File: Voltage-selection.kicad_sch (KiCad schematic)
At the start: 8 parts, among them Q4 DMP1045U-7, Q5 DMP1045U-7, Q6 DMP1045U-7, SW5 SSSS213202

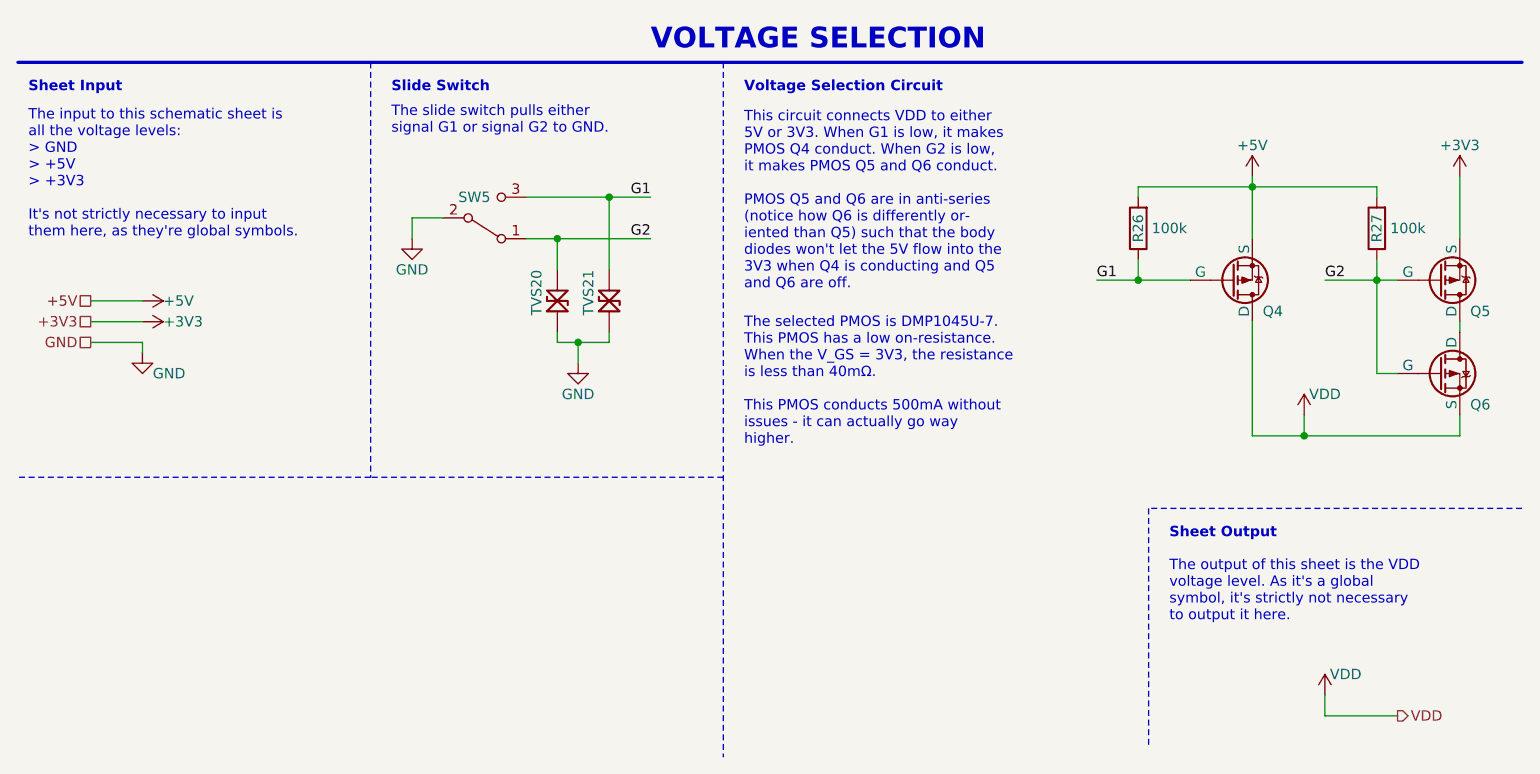
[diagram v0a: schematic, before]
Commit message: Renumber designators and draw new silkscreen
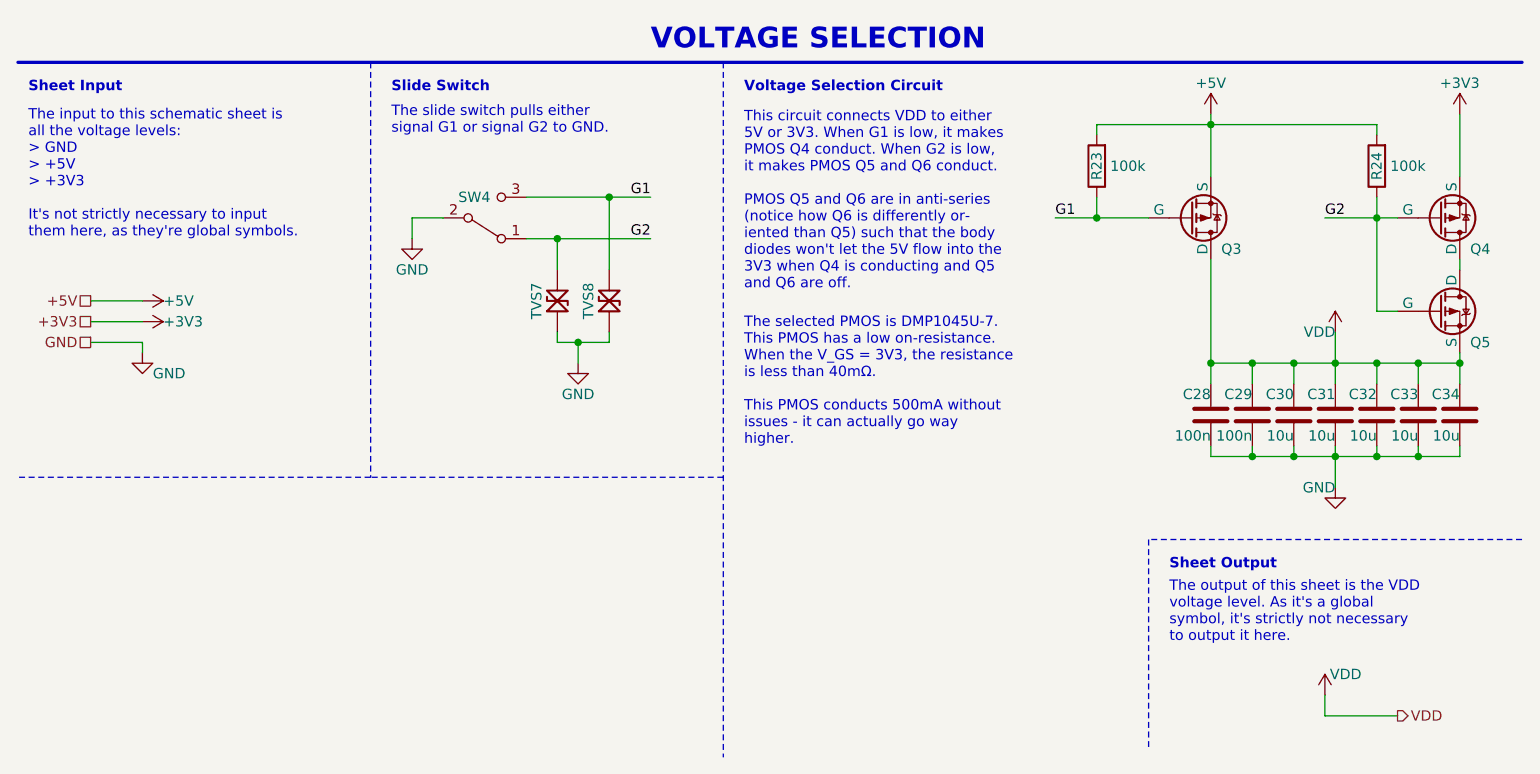
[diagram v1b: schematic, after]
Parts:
- added C28, C29: 100n, Capacitor_SMD:C_0402_1005Metric_Pad0.74x0.62mm_HandSolder, symbol Device:C
- added C30, C31, C32, C33, C34: 10u, Capacitor_SMD:C_0805_2012Metric, symbol Device:C
- renumbered Q4 to Q3, Q5 to Q4, Q6 to Q5, R26 to R23, R27 to R24, SW5 to SW4, TVS20 to TVS7, TVS21 to TVS8
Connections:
- net GND: now also C28.2, C29.2, C30.2, C31.2, C32.2, C33.2, C34.2
- net VDD: now also C28.1, C29.1, C30.1, C31.1, C32.1, C33.1, C34.1
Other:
- moved on the sheet: Q3, Q4, Q5, R23, R24

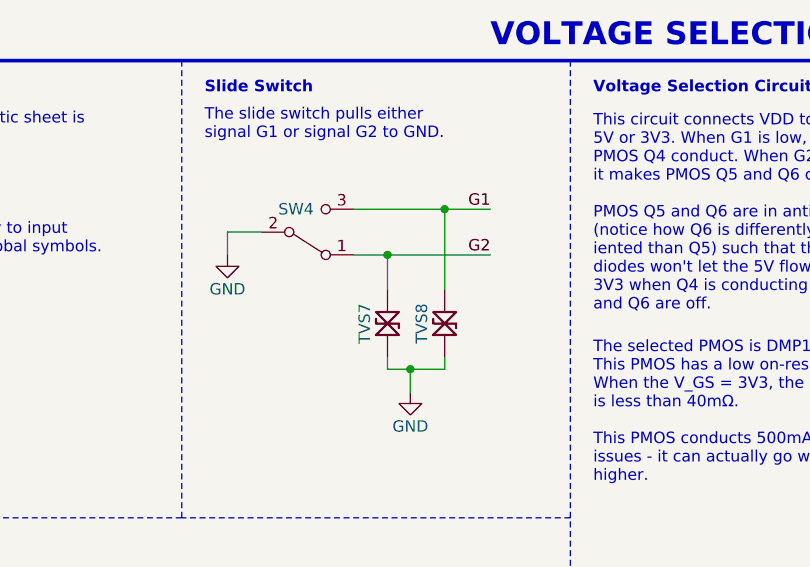
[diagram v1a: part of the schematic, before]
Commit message: Replace TVS diodes with cheaper alternative
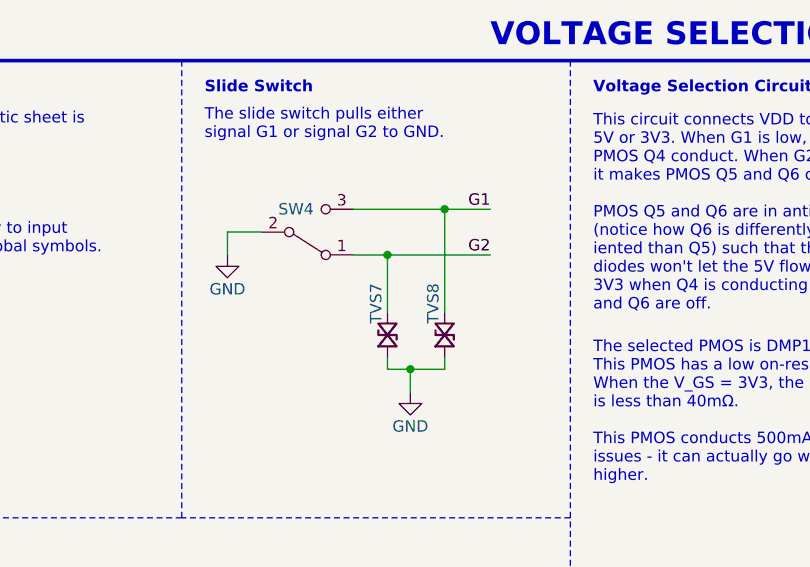
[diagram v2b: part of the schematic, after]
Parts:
- removed TVS7, TVS8: 5V, Tiny_Scarab:D_SOD-323_CDSOD323-T05LC, symbol Tiny_Scarab:CDSOD323-T05LC
- added TVS7, TVS8: 5V, Tiny_Scarab:D_SOD-882_SP1007-01ETG, symbol Tiny_Scarab:TVS_SP1007-01ETG
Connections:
- net G1: now also TVS8.1
- net G2: now also TVS7.1
- net GND: now also TVS7.2, TVS8.2
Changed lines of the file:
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@@
     (stroke (width 0) (type default))
   )
-  (wire (pts (xy 85.09 35.56) (xy 85.09 44.45))
+  (wire (pts (xy 85.09 35.56) (xy 85.09 46.99))
     (stroke (width 0) (type default))
   )
@@
     (stroke (width 0) (type dash))
   )
-  (wire (pts (xy 78.74 40.64) (xy 78.74 44.45))
+  (wire (pts (xy 78.74 40.64) (xy 78.74 46.99))
     (stroke (width 0) (type default))
   )
@@
     )
   )
+  (symbol (lib_id "Tiny_Scarab:TVS_SP1007-01ETG") (at 78.74 49.53 0) (unit 1)
+    (in_bom yes) (on_board yes) (dnp no)
+    (property "Reference" "TVS7" (at 77.47 48.26 90)
+      (effects (font (size 1.27 1.27)) (justify left))
+    )
+    (property "Value" "5V" (at 81.28 50.8 0)
+      (effects (font (size 1.27 1.27)) (justify left) hide)
+    )
+    (property "Footprint" "Tiny_Scarab:D_SOD-882_SP1007-01ETG" (at 67.31 22.86 0)
+      (effects (font (size 1.27 1.27)) (justify left bottom) hide)
+    )
+    (property "Datasheet" "" (at 67.31 25.4 0)
+      (effects (font (size 1.27 1.27)) (justify left) hide)
+    )
+    (property "Manufacturer" "Littelfuse" (at 67.31 29.21 0)
+      (effects (font (size 1.27 1.27)) (justify left bottom) hide)
+    )
+    (property "MPN" "SP1007-01ETG" (at 67.31 31.75 0)
+      (effects (font (size 1.27 1.27)) (justify left bottom) hide)
+    )
+    (property "JLCPCB Part #" "C126836" (at 67.31 34.29 0)
+      (effects (font (size 1.27 1.27)) (justify left) hide)
+    )
+    (property "DigiKey" "F6187TR-ND" (at 67.31 36.83 0)
+      (effects (font (size 1.27 1.27)) (justify left) hide)
+    )
+    (pin "1")
+    (pin "2")
+    (instances
+      (project "tiny-scarab"
+        (path "/156c5422-ee07-49a4-8263-a2dbd26b90bd/481ed0a2-b40b-451f-8f8b-138317026240"
+          (reference "TVS7") (unit 1)
+        )
+      )
+    )
+  )
   (symbol (lib_id "Tiny_Scarab:PMOS_DMP1045U-7") (at 186.69 49.53 0) (unit 1)
     (in_bom yes) (on_board yes) (dnp no)
@@
     )
   )
+  (symbol (lib_id "Tiny_Scarab:TVS_SP1007-01ETG") (at 85.09 49.53 0) (unit 1)
+    (in_bom yes) (on_board yes) (dnp no)
+    (property "Reference" "TVS8" (at 83.82 48.26 90)
+      (effects (font (size 1.27 1.27)) (justify left))
+    )
+    (property "Value" "5V" (at 87.63 50.8 0)
+      (effects (font (size 1.27 1.27)) (justify left) hide)
+    )
+    (property "Footprint" "Tiny_Scarab:D_SOD-882_SP1007-01ETG" (at 73.66 22.86 0)
+      (effects (font (size 1.27 1.27)) (justify left bottom) hide)
+    )
+    (property "Datasheet" "" (at 73.66 25.4 0)
+      (effects (font (size 1.27 1.27)) (justify left) hide)
+    )
+    (property "Manufacturer" "Littelfuse" (at 73.66 29.21 0)
+      (effects (font (size 1.27 1.27)) (justify left bottom) hide)
+    )
+    (property "MPN" "SP1007-01ETG" (at 73.66 31.75 0)
+      (effects (font (size 1.27 1.27)) (justify left bottom) hide)
+    )
+    (property "JLCPCB Part #" "C126836" (at 73.66 34.29 0)
+      (effects (font (size 1.27 1.27)) (justify left) hide)
+    )
+    (property "DigiKey" "F6187TR-ND" (at 73.66 36.83 0)
+      (effects (font (size 1.27 1.27)) (justify left) hide)
+    )
+    (pin "1")
+    (pin "2")
+    (instances
+      (project "tiny-scarab"
+        (path "/156c5422-ee07-49a4-8263-a2dbd26b90bd/481ed0a2-b40b-451f-8f8b-138317026240"
+          (reference "TVS8") (unit 1)
+        )
+      )
+    )
+  )
   (symbol (lib_id "power:GND") (at 60.96 40.64 0) (unit 1)
     (in_bom yes) (on_board yes) (dnp no)
@@
     )
   )
-  (symbol (lib_id "Tiny_Scarab:CDSOD323-T05LC") (at 85.09 48.26 0) (unit 1)
-    (in_bom yes) (on_board yes) (dnp no)
-    (property "Reference" "TVS8" (at 82.55 48.26 90)
-      (effects (font (size 1.27 1.27)))
-    )
-    (property "Value" "5V" (at 86.36 52.07 0)
-      (effects (font (size 0.5 0.5)) (justify left) hide)
-    )
-    (property "Footprint" "Tiny_Scarab:D_SOD-323_CDSOD323-T05LC" (at 95.25 41.91 0)
-      (effects (font (size 1.27 1.27)) (justify left bottom) hide)
-    )
-    (property "Datasheet" "https://www.bourns.com/docs/Product-Datasheets/CDSOD323-TxxLC.pdf" (at 95.25 44.45 0)
-      (effects (font (size 1.27 1.27)) (justify left) hide)
-    )
-    (property "Manufacturer" "Bourns" (at 95.25 48.26 0)
-      (effects (font (size 1.27 1.27)) (justify left bottom) hide)
-    )
-    (property "MPN" "CDSOD323-T05LC" (at 95.25 50.8 0)
-      (effects (font (size 1.27 1.27)) (justify left bottom) hide)
-    )
-    (property "Supplier" "DigiKey" (at 95.25 53.34 0)
-      (effects (font (size 1.27 1.27)) (justify left) hide)
-    )
-    (property "SPN" "CDSOD323-T05LCTR-ND" (at 95.25 55.88 0)
-      (effects (font (size 1.27 1.27)) (justify left) hide)
-    )
-    (property "JLCPCB Part #" "C840637" (at 85.09 48.26 0)
-      (effects (font (size 1.27 1.27)) hide)
-    )
-    (property "DigiKey" "CDSOD323-T05LCTR-ND" (at 73.66 35.56 0)
-      (effects (font (size 1.27 1.27)) (justify left) hide)
-    )
-    (pin "2")
-    (pin "1")
-    (instances
-      (project "tiny-scarab"
-        (path "/156c5422-ee07-49a4-8263-a2dbd26b90bd/481ed0a2-b40b-451f-8f8b-138317026240"
-          (reference "TVS8") (unit 1)
-        )
-      )
-    )
-  )
   (symbol (lib_id "power:+3V3") (at 189.23 25.4 0) (mirror y) (unit 1)
     (in_bom yes) (on_board yes) (dnp no)
@@
         )
       )
-    )
-  )
-  (symbol (lib_id "Tiny_Scarab:CDSOD323-T05LC") (at 78.74 48.26 0) (unit 1)
-    (in_bom yes) (on_board yes) (dnp no)
-    (property "Reference" "TVS7" (at 76.2 48.26 90)
-      (effects (font (size 1.27 1.27)))
-    )
-    (property "Value" "5V" (at 80.01 52.07 0)
-      (effects (font (size 0.5 0.5)) (justify left) hide)
-    )
-    (property "Footprint" "Tiny_Scarab:D_SOD-323_CDSOD323-T05LC" (at 88.9 41.91 0)
-      (effects (font (size 1.27 1.27)) (justify left bottom) hide)
-    )
-    (property "Datasheet" "https://www.bourns.com/docs/Product-Datasheets/CDSOD323-TxxLC.pdf" (at 88.9 44.45 0)
-      (effects (font (size 1.27 1.27)) (justify left) hide)
-    )
-    (property "Manufacturer" "Bourns" (at 88.9 48.26 0)
-      (effects (font (size 1.27 1.27)) (justify left bottom) hide)
-    )
-    (property "MPN" "CDSOD323-T05LC" (at 88.9 50.8 0)
-      (effects (font (size 1.27 1.27)) (justify left bottom) hide)
-    )
-    (property "Supplier" "DigiKey" (at 88.9 53.34 0)
-      (effects (font (size 1.27 1.27)) (justify left) hide)
-    )
-    (property "SPN" "CDSOD323-T05LCTR-ND" (at 88.9 55.88 0)
-      (effects (font (size 1.27 1.27)) (justify left) hide)
-    )
-    (property "JLCPCB Part #" "C840637" (at 78.74 48.26 0)
-      (effects (font (size 1.27 1.27)) hide)
-    )
-    (property "DigiKey" "CDSOD323-T05LCTR-ND" (at 67.31 35.56 0)
-      (effects (font (size 1.27 1.27)) (justify left) hide)
-    )
-    (pin "2")
-    (pin "1")
-    (instances
-      (project "tiny-scarab"
-        (path "/156c5422-ee07-49a4-8263-a2dbd26b90bd/481ed0a2-b40b-451f-8f8b-138317026240"
-          (reference "TVS7") (unit 1)
-        )
-      )

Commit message: Clean up symbols library
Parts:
- Q3, Q4, Q5: DigiKey (none) -> DMP1045U-7DITR-ND; Farnell (none) -> 3127351; Mouser (none) -> 621-DMP1045U-7
- SW4: Farnell (none) -> 3261782; Mouser (none) -> 688-SSSS213202
- TVS7, TVS8: Farnell (none) -> 2777317; Mouser (none) -> 576-SP1007-01ETG
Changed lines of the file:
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@@
       (effects (font (size 1.27 1.27)) (justify left) hide)
+    )
+    (property "Farnell" "2777317" (at 78.74 38.1 0)
+      (effects (font (size 1.27 1.27)) hide)
+    )
+    (property "Mouser" "576-SP1007-01ETG" (at 78.74 40.64 0)
+      (effects (font (size 1.27 1.27)) hide)
     )
     (pin "1")
@@
     )
     (property "JLCPCB Part #" "C177033" (at 186.69 33.02 0)
+      (effects (font (size 1.27 1.27)) hide)
+    )
+    (property "DigiKey" "DMP1045U-7DITR-ND" (at 186.69 34.29 0)
+      (effects (font (size 1.27 1.27)) hide)
+    )
+    (property "Farnell" "3127351" (at 186.69 36.83 0)
+      (effects (font (size 1.27 1.27)) hide)
+    )
+    (property "Mouser" "621-DMP1045U-7" (at 186.69 39.37 0)
       (effects (font (size 1.27 1.27)) hide)
     )
@@
       (effects (font (size 1.27 1.27)) hide)
     )
+    (property "DigiKey" "DMP1045U-7DITR-ND" (at 186.69 53.34 0)
+      (effects (font (size 1.27 1.27)) hide)
+    )
+    (property "Farnell" "3127351" (at 186.69 50.8 0)
+      (effects (font (size 1.27 1.27)) hide)
+    )
+    (property "Mouser" "621-DMP1045U-7" (at 186.69 48.26 0)
+      (effects (font (size 1.27 1.27)) hide)
+    )
     (pin "1")
     (pin "3")
@@
       (effects (font (size 1.27 1.27)) hide)
     )
-    (property "Datasheet" "" (at 69.85 58.42 0)
+    (property "Datasheet" "https://www.farnell.com/datasheets/2864486.pdf" (at 69.85 58.42 0)
       (effects (font (size 1.27 1.27)) hide)
     )
@@
     )
     (property "JLCPCB Part #" "C115375" (at 69.85 45.72 0)
+      (effects (font (size 1.27 1.27)) hide)
+    )
+    (property "DigiKey" "" (at 69.85 38.1 0)
+      (effects (font (size 1.27 1.27)) hide)
+    )
+    (property "Farnell" "3261782" (at 69.85 49.53 0)
+      (effects (font (size 1.27 1.27)) hide)
+    )
+    (property "Mouser" "688-SSSS213202" (at 69.85 46.99 0)
       (effects (font (size 1.27 1.27)) hide)
     )
@@
       (effects (font (size 1.27 1.27)) (justify left) hide)
     )
+    (property "Farnell" "2777317" (at 85.09 38.1 0)
+      (effects (font (size 1.27 1.27)) hide)
+    )
+    (property "Mouser" "576-SP1007-01ETG" (at 85.09 40.64 0)
+      (effects (font (size 1.27 1.27)) hide)
+    )
     (pin "1")
     (pin "2")
@@
       (effects (font (size 1.27 1.27)) hide)
     )
+    (property "DigiKey" "DMP1045U-7DITR-ND" (at 156.21 53.34 0)
+      (effects (font (size 1.27 1.27)) hide)
+    )
+    (property "Farnell" "3127351" (at 156.21 50.8 0)
+      (effects (font (size 1.27 1.27)) hide)
+    )
+    (property "Mouser" "621-DMP1045U-7" (at 156.21 48.26 0)
+      (effects (font (size 1.27 1.27)) hide)
+    )

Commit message: Prefix each symbol name in library - eg. 'D_', 'CONN_', 'IC_', ...
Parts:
- SW4: value SSSS213202 -> 6V 300mA; symbol Tiny_Scarab:SSSS213202 -> Tiny_Scarab:SW_SSSS213202
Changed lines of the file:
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@@
     )
   )
-  (symbol (lib_id "Tiny_Scarab:SSSS213202") (at 69.85 38.1 0) (mirror x) (unit 1)
+  (symbol (lib_id "Tiny_Scarab:SW_SSSS213202") (at 69.85 38.1 0) (mirror x) (unit 1)
     (in_bom yes) (on_board yes) (dnp no)
     (property "Reference" "SW4" (at 68.58 35.56 0)
       (effects (font (size 1.27 1.27)))
     )
-    (property "Value" "SSSS213202" (at 69.85 33.02 0)
+    (property "Value" "6V 300mA" (at 69.85 33.02 0)
       (effects (font (size 1.27 1.27)) hide)
     )
-    (property "Footprint" "Tiny_Scarab:SW_Slide_SPDT_ALPSALPINE_SSSS2" (at 69.85 55.88 0)
+    (property "Footprint" "Tiny_Scarab:SW_Slide_SPDT_ALPSALPINE_SSSS2" (at 69.85 62.23 0)
       (effects (font (size 1.27 1.27)) hide)
     )
-    (property "Datasheet" "https://www.farnell.com/datasheets/2864486.pdf" (at 69.85 58.42 0)
+    (property "Datasheet" "https://www.farnell.com/datasheets/2864486.pdf" (at 69.85 59.69 0)
       (effects (font (size 1.27 1.27)) hide)
     )
-    (property "Manufacturer" "ALPSALPINE" (at 69.85 53.34 0)
+    (property "Manufacturer" "ALPSALPINE" (at 69.85 57.15 0)
       (effects (font (size 1.27 1.27)) hide)
     )
-    (property "MPN" "SSSS213202" (at 69.85 50.8 0)
+    (property "MPN" "SSSS213202" (at 69.85 54.61 0)
       (effects (font (size 1.27 1.27)) hide)
     )
-    (property "JLCPCB Part #" "C115375" (at 69.85 45.72 0)
+    (property "JLCPCB Part #" "C115375" (at 69.85 52.07 0)
       (effects (font (size 1.27 1.27)) hide)
     )

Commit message: Schematic cleanup
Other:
- company: (none) -> Embeetle
- title: (none) -> Tiny Scarab
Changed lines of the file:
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@@
 (kicad_sch (version 20230121) (generator eeschema)
   (paper "A5")
+  (title_block
+    (title "Tiny Scarab")
+    (date "2024-01-30")
+    (rev "0.2")
+    (company "Embeetle")
+    (comment 1 "https://embeetle.com/tiny-scarab")
+    (comment 2 "https://github.com/Embeetle/tiny-scarab")
+  )
   (junction (at 163.83 67.31) (diameter 0) (color 0 0 0 0)
   )
